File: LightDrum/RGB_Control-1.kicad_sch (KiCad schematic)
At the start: 27 parts, among them Q10 PMXB43UNEZ, Q11 PMXB43UNEZ, Q4 PMXB43UNEZ, Q5 PMXB43UNEZ, Q6 PMXB43UNEZ, Q7 PMXB43UNEZ, Q8 PMXB43UNEZ, Q9 PMXB43UNEZ, U9 PCA9634_TSSOP20

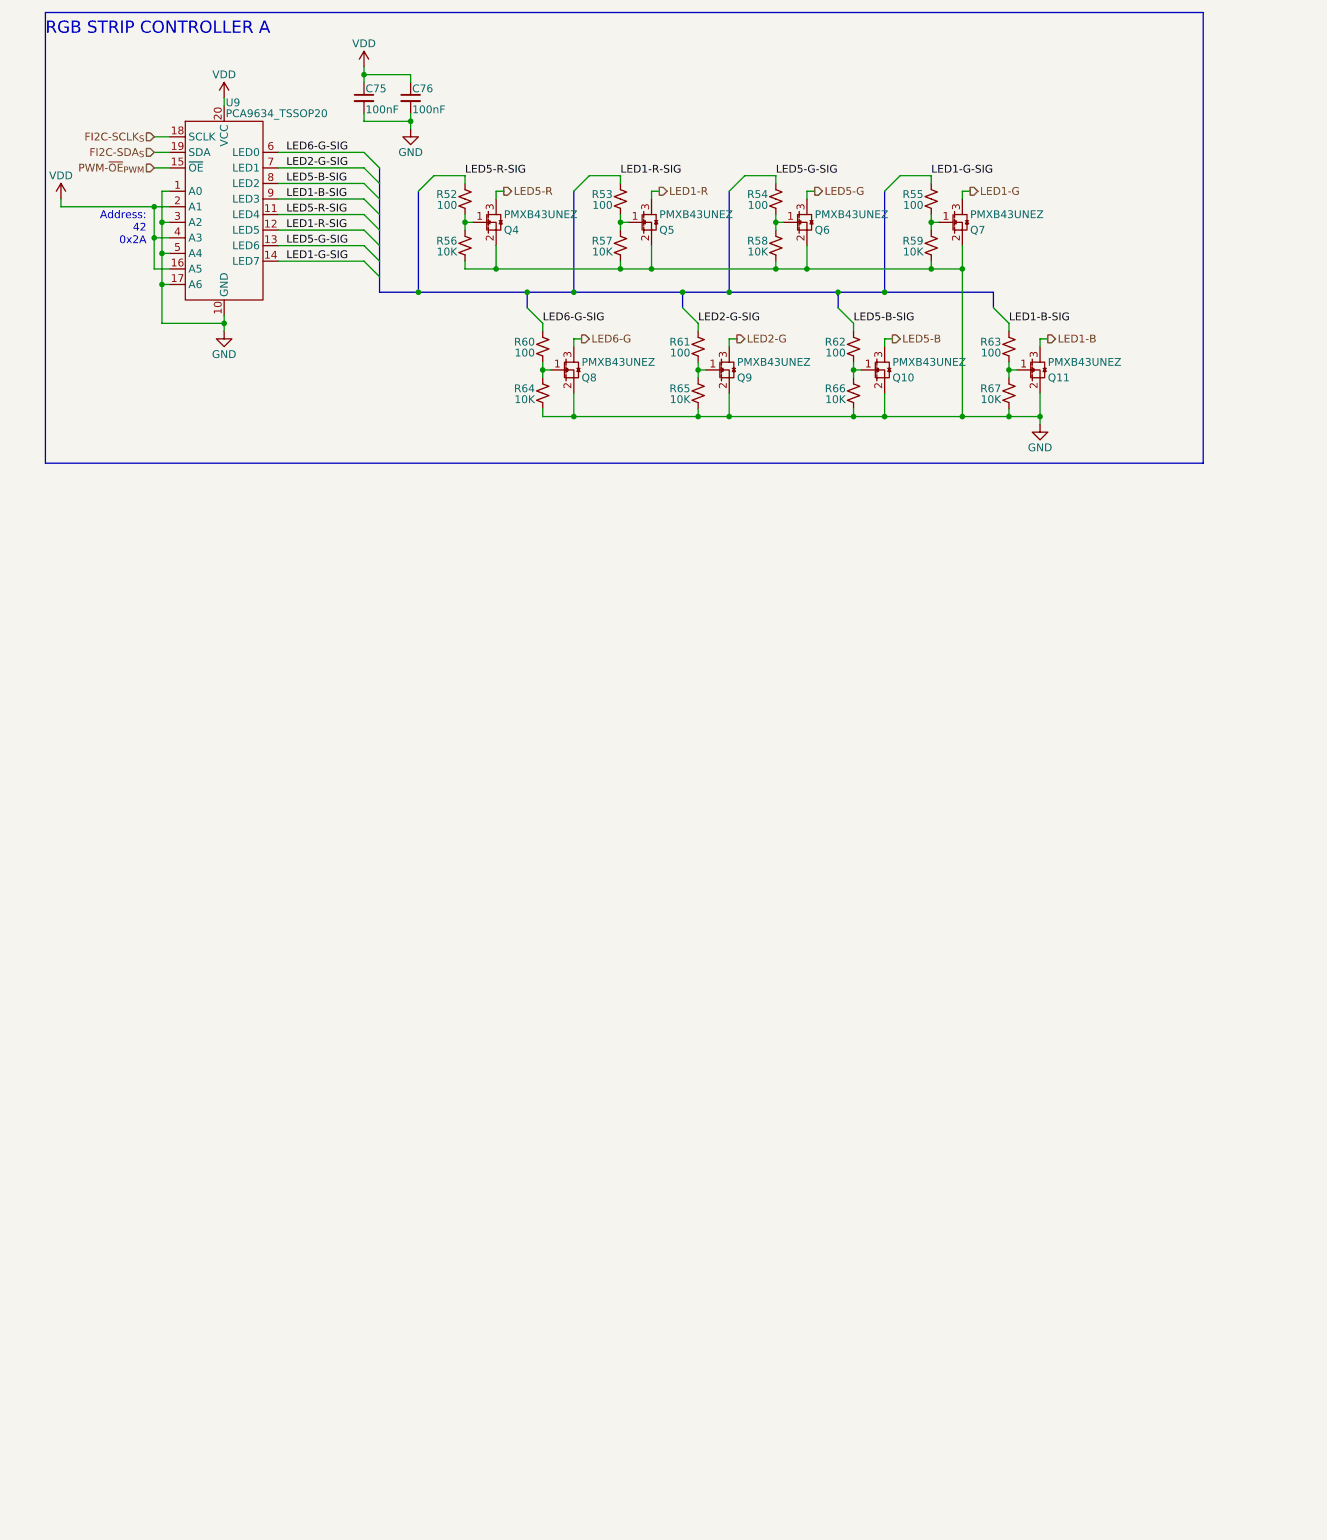
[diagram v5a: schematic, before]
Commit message: Replace DSub with much better ECU conn
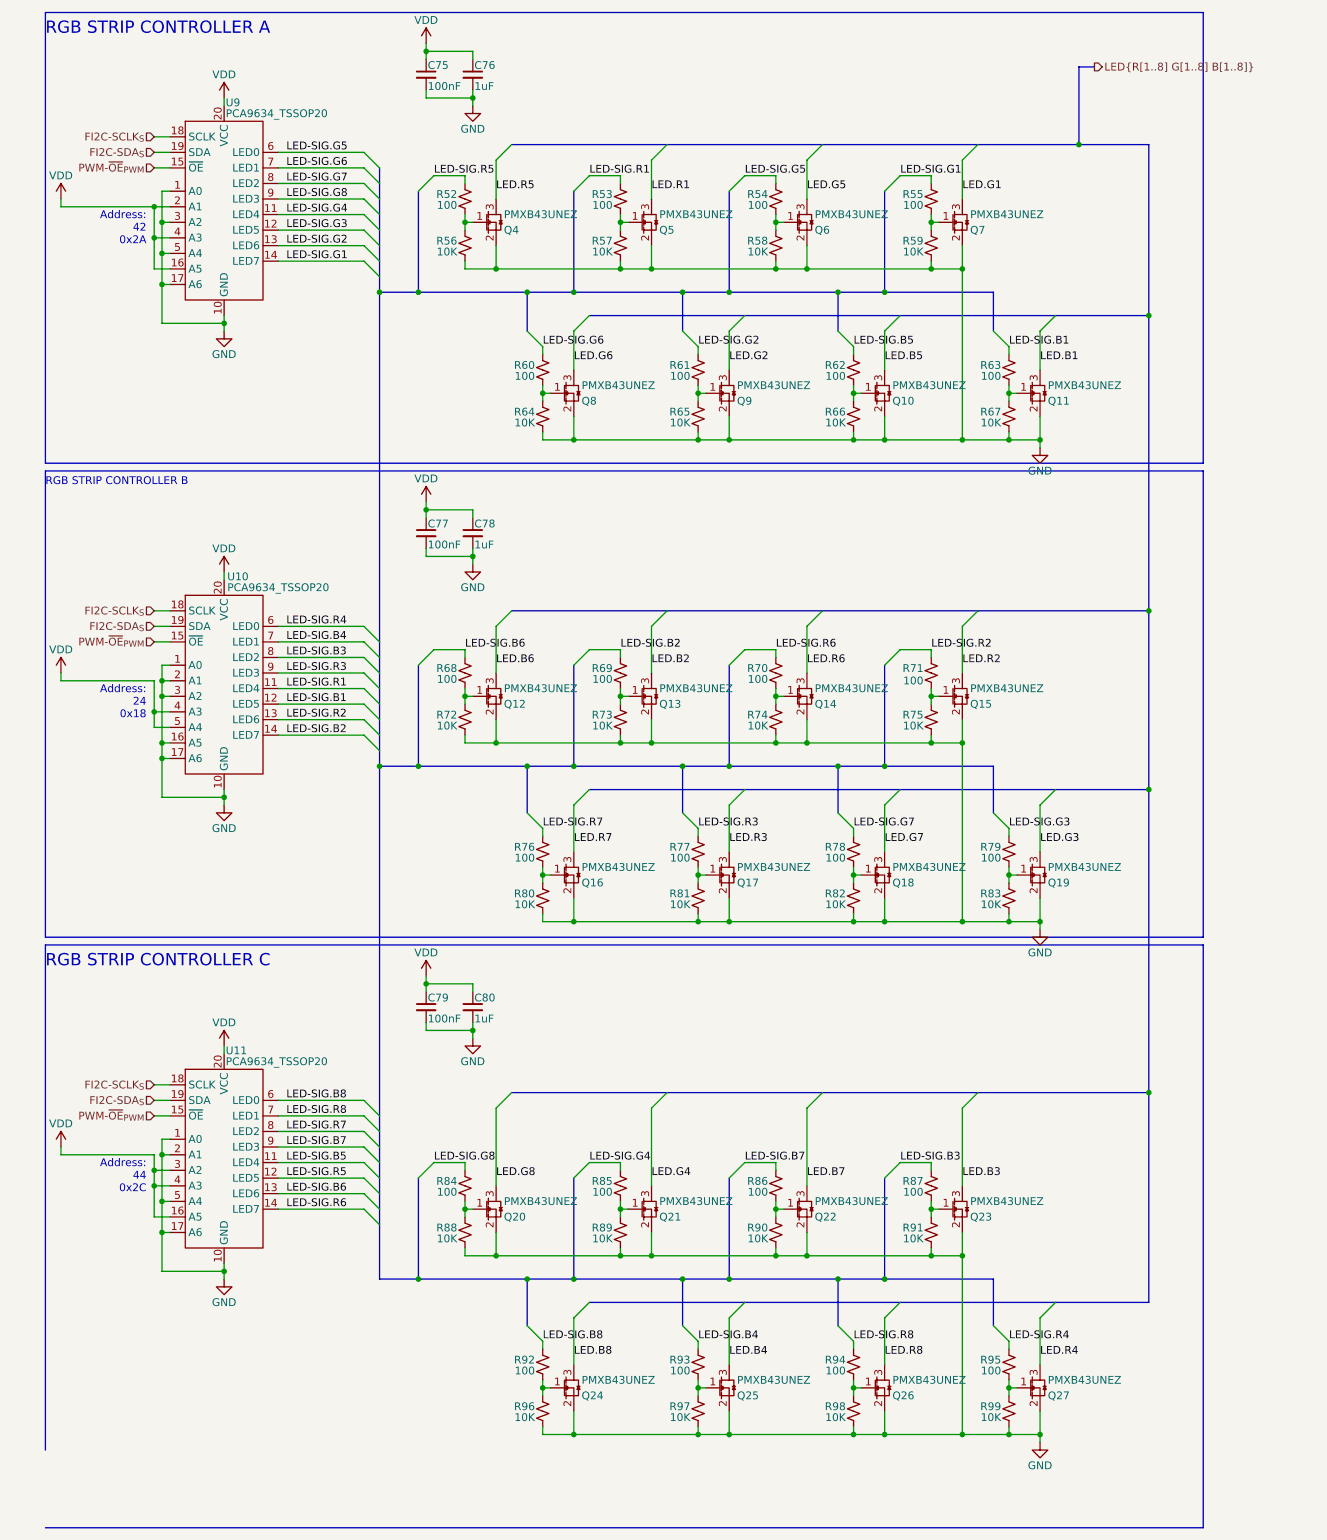
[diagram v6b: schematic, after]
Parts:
- added C77, C79: 100nF, Capacitor_SMD:C_0402_1005Metric, symbol Daxxn_Device:C
- added C78, C80: 1uF, Capacitor_SMD:C_0603_1608Metric, symbol Daxxn_Device:C
- added Q12, Q13, Q14, Q15, Q16, Q17, Q18, Q19, Q20, Q21, Q22, Q23, Q24, Q25, Q26, Q27: PMXB43UNEZ, Daxxn_Packages:DFN1010D-3, symbol Daxxn_Transistors:PMXB43UNEZ
- added R68, R69, R70, R71, R76, R77, R78, R79, R84, R85, R86, R87, R92, R93, R94, R95: 100, Resistor_SMD:R_0402_1005Metric, symbol Device:R_Small_US
- added R72, R73, R74, R75, R80, R81, R82, R83, R88, R89, R90, R91, R96, R97, R98, R99: 10K, Resistor_SMD:R_0402_1005Metric, symbol Device:R_Small_US
- added U10, U11: PCA9634_TSSOP20, Daxxn_Packages:TSSOP-20_4.4x6.5mm_P0.65mm, symbol Daxxn_IC:PCA9634_TSSOP20
- C76: value 100nF -> 1uF; footprint Capacitor_SMD:C_0402_1005Metric -> Capacitor_SMD:C_0603_1608Metric
- U9: footprint Package_SO:TSSOP-20_4.4x6.5mm_P0.65mm -> Daxxn_Packages:TSSOP-20_4.4x6.5mm_P0.65mm
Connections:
- net FI2C-SCLK_{S}: now also U10.18 (SCLK), U11.18 (SCLK)
- net FI2C-SDA_{S}: now also U10.19 (SDA), U11.19 (SDA)
- net GND: now also C77.2, C78.2, C79.2, C80.2, Q12.2 (S), Q13.2 (S), Q14.2 (S), Q15.2 (S), Q16.2 (S), Q17.2 (S), Q18.2 (S), Q19.2 (S), Q20.2 (S), Q21.2 (S), Q22.2 (S), Q23.2 (S), Q24.2 (S), Q25.2 (S), Q26.2 (S), Q27.2 (S), R72.2, R73.2, R74.2, R75.2, R80.2, R81.2, R82.2, R83.2, R88.2, R89.2, R90.2, R91.2, R96.2, R97.2, R98.2, R99.2, U10.1 (A0), U10.10 (GND), U10.16 (A5), U10.17 (A6), U10.2 (A1), U10.3 (A2), U11.1 (A0), U11.10 (GND), U11.17 (A6), U11.2 (A1), U11.5 (A4)
- net PWM-~{OE}_{PWM}: now also U10.15 (~{OE}), U11.15 (~{OE})
- net VDD: now also C77.1, C78.1, C79.1, C80.1, U10.20 (VCC), U10.4 (A3), U10.5 (A4), U11.16 (A5), U11.20 (VCC), U11.3 (A2), U11.4 (A3)
- net LED1-B renamed LED.B1
- net LED1-B-SIG renamed LED-SIG.B1
- net LED-SIG.B1: now also U10.12 (LED5); no longer U9.9 (LED3)
- net LED1-G renamed LED.G1
- net LED1-G-SIG renamed LED-SIG.G1
- net LED1-R renamed LED.R1
- net LED1-R-SIG renamed LED-SIG.G3
- net LED-SIG.G3: now also R79.1; no longer R53.1
- net LED2-G renamed LED.G2
- net LED2-G-SIG renamed LED-SIG.G2
- net LED-SIG.G2: now also U9.13 (LED6); no longer U9.7 (LED1)
- net LED5-B renamed LED.B5
- net LED5-B-SIG renamed LED-SIG.B5
- net LED-SIG.B5: now also U11.11 (LED4); no longer U9.8 (LED2)
- net LED5-G renamed LED.G5
- net LED5-G-SIG renamed LED-SIG.G5
- net LED-SIG.G5: now also U9.6 (LED0); no longer U9.13 (LED6)
- net LED5-R renamed LED.R5
- net LED5-R-SIG renamed LED-SIG.G4
- net LED-SIG.G4: now also R85.1; no longer R52.1
- net LED6-G renamed LED.G6
- net LED6-G-SIG renamed LED-SIG.G6
- net LED-SIG.G6: now also U9.7 (LED1); no longer U9.6 (LED0)
- new net: Q16.1 (G), R76.2, R80.1
- new net: Q25.1 (G), R93.2, R97.1
- new net: Q23.1 (G), R87.2, R91.1
- new net: Q22.1 (G), R86.2, R90.1
- new net: Q15.1 (G), R71.2, R75.1
- new net: Q20.1 (G), R84.2, R88.1
- new net: Q24.1 (G), R92.2, R96.1
- new net: Q17.1 (G), R77.2, R81.1
- new net: Q12.1 (G), R68.2, R72.1
- new net: Q27.1 (G), R95.2, R99.1
- new net: Q14.1 (G), R70.2, R74.1
- new net: Q21.1 (G), R85.2, R89.1
- new net: Q19.1 (G), R79.2, R83.1
- new net: Q13.1 (G), R69.2, R73.1
- new net: Q18.1 (G), R78.2, R82.1
- new net: Q26.1 (G), R94.2, R98.1
- new net LED-SIG.B2: R69.1, U10.14 (LED7)
- new net LED-SIG.B3: R87.1, U10.8 (LED2)
- new net LED-SIG.B4: R93.1, U10.7 (LED1)
- new net LED-SIG.B6: R68.1, U11.13 (LED6)
- new net LED-SIG.B7: R86.1, U11.9 (LED3)
- new net LED-SIG.B8: R92.1, U11.6 (LED0)
- new net LED-SIG.G7: R78.1, U9.8 (LED2)
- new net LED-SIG.G8: R84.1, U9.9 (LED3)
- new net LED-SIG.R1: R53.1, U10.11 (LED4)
- new net LED-SIG.R2: R71.1, U10.13 (LED6)
- new net LED-SIG.R3: R77.1, U10.9 (LED3)
- new net LED-SIG.R4: R95.1, U10.6 (LED0)
- new net LED-SIG.R5: R52.1, U11.12 (LED5)
- new net LED-SIG.R6: R70.1, U11.14 (LED7)
- new net LED-SIG.R7: R76.1, U11.8 (LED2)
- new net LED-SIG.R8: R94.1, U11.7 (LED1)
- new net LED.B2: Q13.3 (D)
- new net LED.B3: Q23.3 (D)
- new net LED.B4: Q25.3 (D)
- new net LED.B6: Q12.3 (D)
- new net LED.B7: Q22.3 (D)
- new net LED.B8: Q24.3 (D)
- new net LED.G3: Q19.3 (D)
- new net LED.G4: Q21.3 (D)
- new net LED.G7: Q18.3 (D)
- new net LED.G8: Q20.3 (D)
- new net LED.R2: Q15.3 (D)
- new net LED.R3: Q17.3 (D)
- new net LED.R4: Q27.3 (D)
- new net LED.R6: Q14.3 (D)
- new net LED.R7: Q16.3 (D)
- new net LED.R8: Q26.3 (D)
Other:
- note added: "Address: 24 0x18"
- note added: "Address: 44 0x2C"
- note added: "RGB STRIP CONTROLLER B"
- note added: "RGB STRIP CONTROLLER C"
- moved on the sheet: C75, C76, Q10, Q11, Q8, Q9, R60, R61, R62, R63, R64, R65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

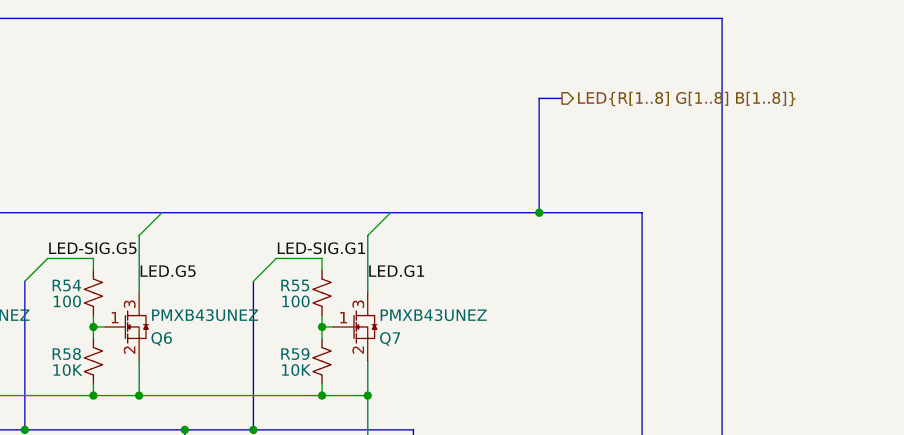
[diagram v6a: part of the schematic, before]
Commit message: Organize old files and generate interface gerbers
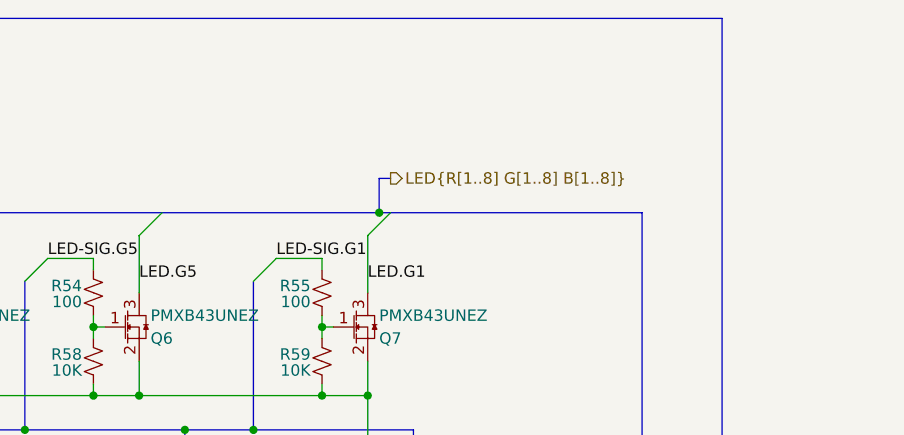
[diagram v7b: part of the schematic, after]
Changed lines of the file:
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@@
   (junction (at 161.29 50.8) (diameter 0) (color 0 0 0 0)
   )
-  (junction (at 185.42 38.1) (diameter 0) (color 0 0 0 0)
-  )
   (junction (at 161.29 135.89) (diameter 0) (color 0 0 0 0)
   )
@@
   (junction (at 35.56 215.9) (diameter 0) (color 0 0 0 0)
   )
+  (junction (at 167.64 38.1) (diameter 0) (color 0 0 0 0)
+  )
   (junction (at 148.59 165.1) (diameter 0) (color 0 0 0 0)
   )
@@
     (stroke (width 0) (type default))
   )
-  (bus (pts (xy 143.51 38.1) (xy 168.91 38.1))
+  (bus (pts (xy 143.51 38.1) (xy 167.64 38.1))
     (stroke (width 0) (type default))
   )
@@
     (stroke (width 0) (type default))
   )
+  (bus (pts (xy 168.91 38.1) (xy 196.85 38.1))
+    (stroke (width 0) (type default))
+  )
   (wire (pts (xy 140.97 135.89) (xy 161.29 135.89))
     (stroke (width 0) (type default))
@@
     (stroke (width 0) (type default))
   )
-  (bus (pts (xy 185.42 38.1) (xy 196.85 38.1))
-    (stroke (width 0) (type default))
-  )
   (bus (pts (xy 71.12 52.07) (xy 71.12 54.61))
     (stroke (width 0) (type default))
@@
     (stroke (width 0) (type default))
   )
-  (bus (pts (xy 168.91 38.1) (xy 185.42 38.1))
-    (stroke (width 0) (type default))
-  )
   (bus (pts (xy 71.12 119.38) (xy 71.12 121.92))
     (stroke (width 0) (type default))
@@
     (stroke (width 0) (type default))
   )
+  (bus (pts (xy 167.64 38.1) (xy 168.91 38.1))
+    (stroke (width 0) (type default))
+  )
   (wire (pts (xy 90.17 58.42) (xy 110.49 58.42))
     (stroke (width 0) (type default))
@@
     (stroke (width 0) (type default))
   )
-  (bus (pts (xy 187.96 25.4) (xy 185.42 25.4))
+  (bus (pts (xy 168.91 34.29) (xy 167.64 34.29))
     (stroke (width 0) (type default))
   )
@@
     (stroke (width 0) (type default))
   )
-  (bus (pts (xy 185.42 25.4) (xy 185.42 38.1))
+  (bus (pts (xy 167.64 34.29) (xy 167.64 38.1))
     (stroke (width 0) (type default))
   )
@@
     (effects (font (size 1.27 1.27)) (justify right))
   )
-  (hierarchical_label "LED{R[1..8] G[1..8] B[1..8]}" (shape output) (at 187.96 25.4 0) (fields_autoplaced)
+  (hierarchical_label "LED{R[1..8] G[1..8] B[1..8]}" (shape output) (at 168.91 34.29 0) (fields_autoplaced)
     (effects (font (size 1.27 1.27)) (justify left))
   )
